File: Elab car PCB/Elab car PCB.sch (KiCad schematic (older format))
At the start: 63 parts, among them J1 USB_B, J10 Conn_01x04, J11 Screw_Terminal_01x02, J12 Screw_Terminal_01x02, J2 Screw_Terminal_01x02, J3 Screw_Terminal_01x02, J4 Screw_Terminal_01x02, J5 Conn_01x04, J6 Conn_01x03, J7 Conn_01x03, J8 Conn_01x03, J9 Conn_01x08, Q1 S8050, Q2 S8050, SW1 SW_Push, SW2 SW_Push, SW3 SW_Push, U1 CH340G, U2 L293D, U3 AMS1117-3.3, U4 ESP32-WROOM-32, U5 L7805, Y1 12MHz

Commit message: Assignation d'empreintes
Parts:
- removed D1, D16, D18, D2: D_Shockley, symbol Device:D_Shockley
- removed D10, D20, D3, D4, D5, D6, D7, D8, D9: D, symbol Device:D
- added C7: 0.1µF/100nF, Capacitor_SMD:C_1206_3216Metric_Pad1.33x1.80mm_HandSolder, symbol Device:C
- added D1, D10, D16, D18, D2, D20, D3, D4, D5, D6, D7, D8, D9: D_Schottky, Diode_SMD:D_0805_2012Metric_Pad1.15x1.40mm_HandSolder, symbol Device:D_Schottky
- C1, C2: value 22p -> 20p; footprint (none) -> Capacitor_SMD:C_1206_3216Metric_Pad1.33x1.80mm_HandSolder
- C3, C6: footprint (none) -> Capacitor_SMD:CP_Elec_5x4.5
- C4: footprint (none) -> Capacitor_SMD:CP_Elec_5x5.3
- C5: footprint (none) -> Capacitor_SMD:CP_Elec_6.3x5.8
- D15: value LED -> LED_BUILTIN; footprint (none) -> LED_SMD:LED_0805_2012Metric_Pad1.15x1.40mm_HandSolder
- D17: value LED -> LED_3.3V; footprint (none) -> LED_SMD:LED_0805_2012Metric_Pad1.15x1.40mm_HandSolder
- D19: value LED -> LED_5V; footprint (none) -> LED_SMD:LED_0805_2012Metric_Pad1.15x1.40mm_HandSolder
- F1: footprint (none) -> Fuse:Fuse_1206_3216Metric_Pad1.42x1.75mm_HandSolder
- J1: footprint (none) -> Connector_USB:USB_B_Lumberg_2411_02_Horizontal
- J10, J5: footprint (none) -> Connector_PinHeader_2.54mm:PinHeader_1x04_P2.54mm_Vertical
- J11, J12, J2, J3, J4: footprint (none) -> TerminalBlock:TerminalBlock_bornier-2_P5.08mm
- J6, J7, J8: footprint (none) -> Connector_PinHeader_2.54mm:PinHeader_1x03_P2.54mm_Vertical
- J9: footprint (none) -> Connector_PinHeader_2.54mm:PinHeader_1x08_P2.54mm_Vertical
- R1, R5: value 65 -> 20; footprint (none) -> Resistor_SMD:R_1206_3216Metric_Pad1.30x1.75mm_HandSolder
- R11, R12, R13, R2, R3, R4: footprint (none) -> Resistor_SMD:R_1206_3216Metric_Pad1.30x1.75mm_HandSolder
- R6: value 220 -> 100; footprint (none) -> Resistor_SMD:R_1206_3216Metric_Pad1.30x1.75mm_HandSolder
- R7, R8: value R -> 12k; footprint (none) -> Resistor_SMD:R_1206_3216Metric_Pad1.30x1.75mm_HandSolder
- SW1, SW2, SW3: footprint (none) -> Button_Switch_SMD:SW_Push_1P1T_NO_6x6mm_H9.5mm
- U5: footprint (none) -> Package_TO_SOT_SMD:TO-263-3_TabPin4
- Y1: footprint (none) -> Crystal:Crystal_SMD_3225-4Pin_3.2x2.5mm_HandSoldering
- gave numbers to parts that had none: 2
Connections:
- net labels removed: RST, mot_en
- wire segments 183 -> 188
- no-connect marks 19 -> 24

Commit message: Ajout de références
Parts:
- C1, C2: value 20p -> 20pF; LCSC # (none) -> C1894; Référence (none) -> 1206CG200J500NT
- C3: LCSC # (none) -> C249788; Référence (none) -> VSS100M1ETR-0504
- C4: LCSC # (none) -> C371125; Référence (none) -> BXA25VC22M5*5_5.0TP
- C5: value 47µ -> 47µF; LCSC # (none) -> C311639; Référence (none) -> VZL470M1ETR-0606
- C6: value 10µ -> 10µF; LCSC # (none) -> C249788; Référence (none) -> VSS100M1ETR-0504
- C7: value 0.1µF/100nF -> 100nF; LCSC # (none) -> C107181; Référence (none) -> CC1206KKX7R0BB104
- D1, D10, D16, D18, D2, D20, D3, D4, D5, D6, D7, D8, D9: LCSC # (none) -> C189958; Référence (none) -> MSCD104H
- D11, D12, D13, D14: LCSC # (none) -> C114586; Référence (none) -> WS2812B-B
- D15: value LED_BUILTIN -> Blue_led; LCSC # (none) -> C72035; Référence (none) -> 17-21/BHC-XL2M2TY/3T
- D17: value LED_3.3V -> Blue_led; LCSC # (none) -> C72035; Référence (none) -> 17-21/BHC-XL2M2TY/3T
- D19: value LED_5V -> Blue_led; LCSC # (none) -> C72035; Référence (none) -> 17-21/BHC-XL2M2TY/3T
- F1: LCSC # (none) -> C70070; Référence (none) -> nSMD025-30V
- J1: LCSC # (none) -> C397338; Référence (none) -> U241-041N-1BR85-1
- J10, J5: LCSC # (none) -> C124413; Référence (none) -> C124413
- J11, J12, J2, J3, J4: LCSC # (none) -> C8465; Référence (none) -> WJ500V-5.08-2P
- J6, J7, J8: LCSC # (none) -> C225500; Référence (none) -> A2541HWV-3P
- J9: LCSC # (none) -> C27438; Référence (none) -> C27438
- Q1, Q2: footprint Package_TO_SOT_THT:TO-92_Inline -> Package_TO_SOT_SMD:SOT-23_Handsoldering; LCSC # (none) -> C402279; Référence (none) -> S8050
- Q3, Q4: LCSC # (none) -> C9114; Référence (none) -> 2N7000
- R1, R5: value 20 -> 20R; LCSC # (none) -> C25362; Référence (none) -> 1206W4J0200T5E
- R11, R12, R13, R2, R3, R4, R7, R8: LCSC # (none) -> C1491; Référence (none) -> 1206W4J0123T5E
- R6: value 100 -> 100R; LCSC # (none) -> C242479; Référence (none) -> CRCW1206100RFKEA
- SW1, SW2, SW3: LCSC # (none) -> C111373; Référence (none) -> TS-1102W-4316
- U1: LCSC # (none) -> C14267; Référence (none) -> CH340G
- U2: LCSC # (none) -> C12340; Référence (none) -> L293D
- U3: LCSC # (none) -> C369933; Référence (none) -> AMS1117-3.3
- U4: LCSC # (none) -> C473012; Référence (none) -> ESP32-WROOM-32D
- U5: LCSC # (none) -> C507146; Référence (none) -> LM7805S/TR
- Y1: LCSC # (none) -> C164041; Référence (none) -> TAXM12M4RDBCCT2T

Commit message: PCB creation
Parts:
- removed Y1: 12MHz, Crystal:Crystal_SMD_3225-4Pin_3.2x2.5mm_HandSoldering, symbol Device:Crystal
- added Y1: Crystal_GND24, Crystal:Crystal_SMD_3225-4Pin_3.2x2.5mm_HandSoldering, symbol Device:Crystal_GND24
- D1, D10, D16, D18, D2, D20, D3, D4, D5, D6, D7, D8, D9: footprint Diode_SMD:D_0805_2012Metric_Pad1.15x1.40mm_HandSolder -> Diode_SMD:D_1206_3216Metric_Pad1.42x1.75mm_HandSolder
- D17: value Blue_led -> 3.3V PWR
- D19: value Blue_led -> 5V PWR
- R1: value 20R -> 85R
- R6: value 100R -> 85r
- SW1, SW2, SW3: footprint Button_Switch_SMD:SW_Push_1P1T_NO_6x6mm_H9.5mm -> Button_Switch_THT:SW_PUSH_6mm_H5mm
- U5: footprint Package_TO_SOT_SMD:TO-263-3_TabPin4 -> Package_TO_SOT_SMD:TO-263-2
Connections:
- net BP_1: now also U4.7 (IO35); no longer U4.6 (IO34)
- net BP_2: now also U4.8 (IO32); no longer U4.7 (IO35)
- net GND: now also D10.2 (A), Y1.2, Y1.4
- net WS_sig: now also U4.6 (IO34); no longer U4.16 (IO13)
- net dist_sensor: now also U4.10 (IO25); no longer U4.13 (IO14)
- net line_sens_1: now also U4.9 (IO33); no longer U4.10 (IO25)
- net mot1back: now also U4.31 (IO19); no longer U4.30 (IO18)
- net mot1en: now also U4.29 (IO5); no longer U4.26 (IO4)
- net mot1for: now also U4.30 (IO18); no longer U4.27 (IO16)
- net mot2back: now also U4.28 (IO17); no longer U4.31 (IO19)
- net mot2en: now also U4.26 (IO4); no longer U4.29 (IO5)
- net mot2for: now also U4.27 (IO16); no longer U4.28 (IO17)
- net mot_pwr: now also D3.1 (K), D5.1 (K)
- net servo_sig: now also U4.13 (IO14); no longer U4.9 (IO33)
- net D+: now reaches J1.3 (D+), U1.5 (UD+)
- net D-: now reaches J1.2 (D-), U1.6 (UD-)
- net at C1.1, U1.7 (XI): now also Y1.1
- net at C2.1, U1.8 (XO): now also Y1.3

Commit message: Silk screen
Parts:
- added TP1, TP10, TP11, TP12, TP13, TP14, TP15, TP16, TP17, TP18, TP19, TP2, TP20, TP21, TP22, TP3, TP4, TP5, TP6, TP7, TP8, TP9: TestPoint, TestPoint:TestPoint_Pad_D2.5mm, symbol Connector:TestPoint
- D10, D3, D4, D5, D6, D7, D8, D9: value D_Schottky -> Flyback
- D15: value Blue_led -> LED_BUILTIN
- J10: value Conn_01x04 -> I2C
- J11: value Screw_Terminal_01x02 -> SCL pullup
- J12: value Screw_Terminal_01x02 -> SDA pullup
- J2: value Screw_Terminal_01x02 -> Power input
- J3: value Screw_Terminal_01x02 -> L_Mot
- J4: value Screw_Terminal_01x02 -> R_Mot
- J5: value Conn_01x04 -> HC-SR04
- J6: value Conn_01x03 -> R_Line
- J7: value Conn_01x03 -> L_Line
- J8: value Conn_01x03 -> Servo
- J9: value Conn_01x08 -> MPU5060
- SW1: value SW_Push -> Reset
- SW2: value SW_Push -> User 1
- SW3: value SW_Push -> User 2
- Y1: value Crystal_GND24 -> 12MHz
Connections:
- net +3V3: now also TP4.1
- net +5V: now also TP5.1
- net BP_1: now also TP8.1
- net BP_2: now also TP15.1
- net D+: now also TP2.1
- net D-: now also TP3.1
- net SCL: now also TP20.1
- net SDA: now also TP19.1
- net dist_sensor: now also TP6.1
- net esp_EN: now also TP18.1
- net esp_IO0: now also TP17.1
- net esp_SCL: now also TP22.1
- net esp_SDA: now also TP21.1
- net line_sens_1: now also TP7.1
- net line_sens_2: now also TP9.1
- net servo_sig: now also TP10.1
- net at D10.1 (K), D9.2 (A), J4.1 (Pin_1)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: now also TP13.1
- net at D5.2 (A), D6.1 (K), J4.2 (Pin_2)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: now also TP14.1
- net at D7.2 (A), D8.1 (K), J3.1 (Pin_1)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: now also TP11.1
- net at D3.2 (A), D4.1 (K), J3.2 (Pin_2)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: now also TP12.1
- net at D2.2 (A), J2.2 (Pin_2): now also TP1.1
- net at D20.1 (K), Q1.3 (C): now also TP16.1

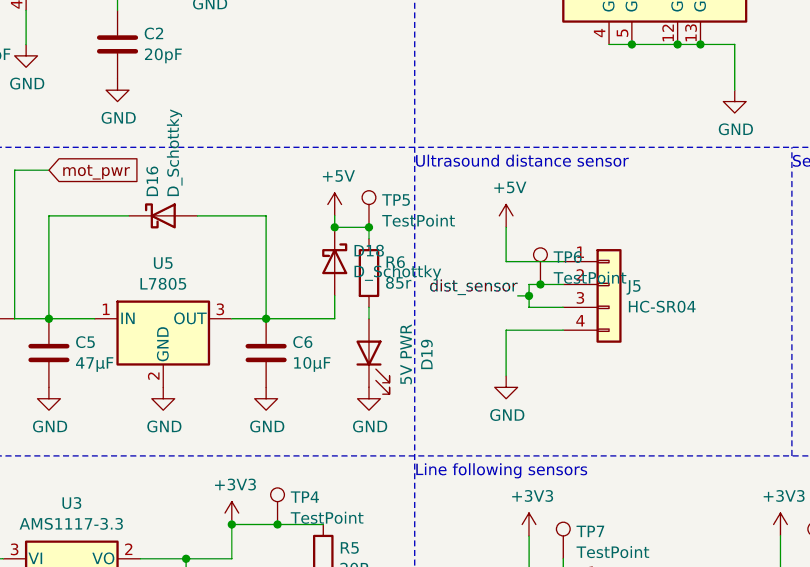
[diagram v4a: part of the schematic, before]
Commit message: Esp32 design requirements corrections
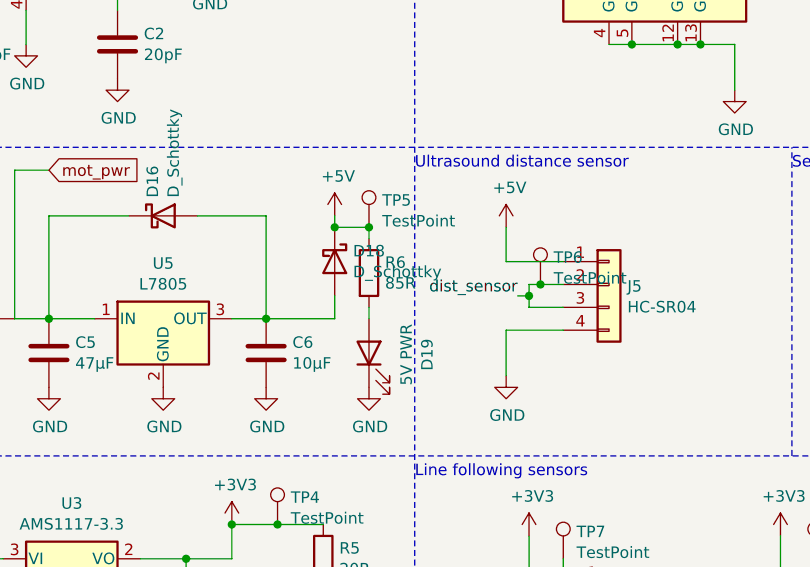
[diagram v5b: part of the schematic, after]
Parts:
- R6: value 85r -> 85R
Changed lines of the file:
@@
 P 3350 3950
 F 0 "R6" H 3420 3996 50  0000 L CNN
-F 1 "85r" H 3420 3905 50  0000 L CNN
+F 1 "85R" H 3420 3905 50  0000 L CNN
 F 2 "Resistor_SMD:R_1206_3216Metric_Pad1.30x1.75mm_HandSolder" V 3280 3950 50  0001 C CNN
 F 3 "~" H 3350 3950 50  0001 C CNN

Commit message: V1.1
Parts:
- removed J6: R_Line, Connector_PinHeader_2.54mm:PinHeader_1x03_P2.54mm_Vertical, symbol Connector_Generic:Conn_01x03
- removed J7: L_Line, Connector_PinHeader_2.54mm:PinHeader_1x03_P2.54mm_Vertical, symbol Connector_Generic:Conn_01x03
- removed Q1, Q2: S8050, Package_TO_SOT_SMD:SOT-23_Handsoldering, symbol Transistor_BJT:S8050
- removed TP1, TP11, TP12, TP13, TP14, TP16, TP2, TP3: TestPoint, TestPoint:TestPoint_Pad_D2.5mm, symbol Connector:TestPoint
- added H1, H2, H3, H4: MountingHole, MountingHole:MountingHole_3.2mm_M3_DIN965_Pad, symbol Mechanical:MountingHole
- added J13: Conn_01x03, Connector_PinHeader_2.54mm:PinHeader_1x03_P2.54mm_Vertical, symbol Connector_Generic:Conn_01x03
- added J6, J7: Conn_01x04, Connector_PinHeader_2.54mm:PinHeader_1x04_P2.54mm_Vertical, symbol Connector_Generic:Conn_01x04
- added Q1, Q2: S8050, Package_TO_SOT_SMD:SOT-23_Handsoldering, symbol Transistor_BJT:2N3055
- added SW4: SW_DIP_x01, electroLABOT_switch:SW_plugin8.5x8.5, symbol Switch:SW_DIP_x01
- R1: value 85R -> 20R
- R5: value 20R -> 100R
- R6: value 85R -> 200R
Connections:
- net +3V3: now also J6.4 (Pin_4), J7.4 (Pin_4)
- net +5V: now also J8.2 (Pin_2); no longer J8.1 (Pin_1)
- net BP_1: now also U4.9 (IO33); no longer U4.7 (IO35)
- net BP_2: now also U4.10 (IO25); no longer U4.8 (IO32)
- net DTR: now also Q2.2 (E)
- net GND: now also J13.3 (Pin_3), J6.3 (Pin_3), J7.3 (Pin_3)
- net RTS: now also Q1.2 (E)
- net WS_sig: now also U4.8 (IO32); no longer U4.6 (IO34)
- net dist_sensor: now also U4.12 (IO27); no longer U4.10 (IO25)
- net esp_IO0: now also Q2.3 (C)
- net line_sens_1: now also U4.11 (IO26), J6.1 (Pin_1); no longer U4.9 (IO33)
- net line_sens_2: now also U4.13 (IO14), J7.1 (Pin_1); no longer U4.11 (IO26)
- net servo_sig: now also J8.1 (Pin_1), U4.16 (IO13); no longer J8.2 (Pin_2), U4.13 (IO14)
- net piezo: now reaches U4.23 (IO15)
- net piezo: now also J13.1 (Pin_1)
- net at J2.2 (Pin_2): now also SW4.1; no longer D2.2 (A)
- net at R8.2: now also Q2.1 (B)
- net at R7.2: now also Q1.1 (B)
- net at D20.1 (K): now also Q1.3 (C)
- new net: D2.2 (A), SW4.2
- no-connect marks 24 -> 25
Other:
- note added: "Mounting holes"
- moved on the sheet: J2, TP10, TP7, TP9

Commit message: Little corrections of V1.1
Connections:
- net +5V: now also J13.2 (Pin_2)
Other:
- moved on the sheet: J13
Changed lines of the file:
@@
 L power:GND #PWR0103
 U 1 1 6209DD59
-P 8300 5450
-F 0 "#PWR0103" H 8300 5200 50  0001 C CNN
-F 1 "GND" H 8305 5277 50  0000 C CNN
-F 2 "" H 8300 5450 50  0001 C CNN
-F 3 "" H 8300 5450 50  0001 C CNN
-	1    8300 5450
+P 8350 5450
+F 0 "#PWR0103" H 8350 5200 50  0001 C CNN
+F 1 "GND" H 8355 5277 50  0000 C CNN
+F 2 "" H 8350 5450 50  0001 C CNN
+F 3 "" H 8350 5450 50  0001 C CNN
+	1    8350 5450
 	1    0    0    -1
 $EndComp
 Wire Wire Line
-	8450 5350 8300 5350
+	8500 5350 8350 5350
 Wire Wire Line
-	8300 5350 8300 5450
-Text Label 8450 5150 2    50   ~ 0
+	8350 5350 8350 5450
+Text Label 8500 5150 2    50   ~ 0
 piezo
 Text Label 10350 4050 0    50   ~ 0
@@
 L Connector_Generic:Conn_01x03 J13
 U 1 1 620D3207
-P 8650 5250
-F 0 "J13" H 8730 5292 50  0000 L CNN
-F 1 "Conn_01x03" H 8730 5201 50  0000 L CNN
-F 2 "Connector_PinHeader_2.54mm:PinHeader_1x03_P2.54mm_Vertical" H 8650 5250 50  0001 C CNN
-F 3 "~" H 8650 5250 50  0001 C CNN
-	1    8650 5250
+P 8700 5250
+F 0 "J13" H 8780 5292 50  0000 L CNN
+F 1 "Conn_01x03" H 8780 5201 50  0000 L CNN
+F 2 "Connector_PinHeader_2.54mm:PinHeader_1x03_P2.54mm_Vertical" H 8700 5250 50  0001 C CNN
+F 3 "~" H 8700 5250 50  0001 C CNN
+	1    8700 5250
 	1    0    0    -1
 $EndComp
@@
 Wire Wire Line
 	800  4150 900  4150
+$Comp
+L power:+5V #PWR0104
+U 1 1 61C21E0C
+P 8200 5200
+F 0 "#PWR0104" H 8200 5050 50  0001 C CNN
+F 1 "+5V" H 8215 5373 50  0000 C CNN
+F 2 "" H 8200 5200 50  0001 C CNN
+F 3 "" H 8200 5200 50  0001 C CNN
+	1    8200 5200
+	1    0    0    -1
+$EndComp
+Wire Wire Line
+	8200 5250 8500 5250
+Wire Wire Line
+	8200 5200 8200 5250
 $EndSCHEMATC
